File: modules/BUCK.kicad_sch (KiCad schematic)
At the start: 6 parts, among them U4 TPS628502

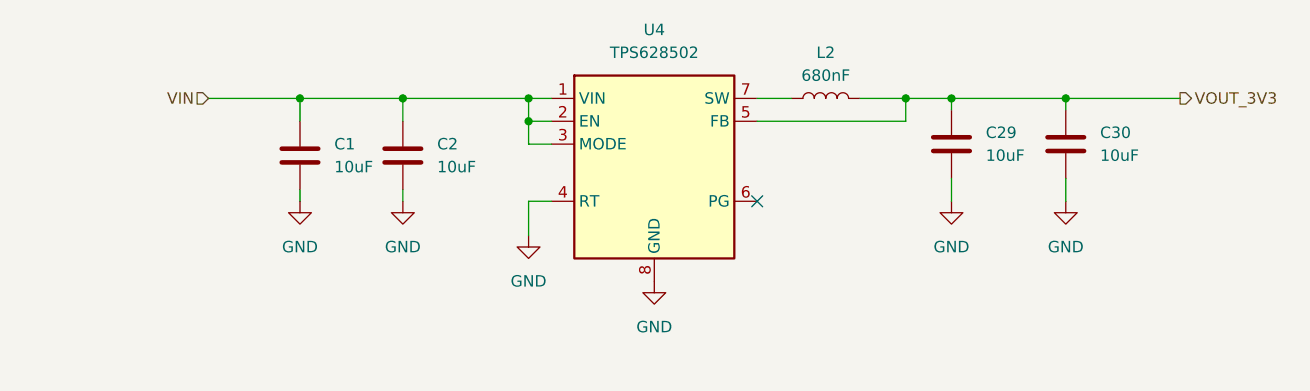
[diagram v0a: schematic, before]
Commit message: Modificaciond de conexiones
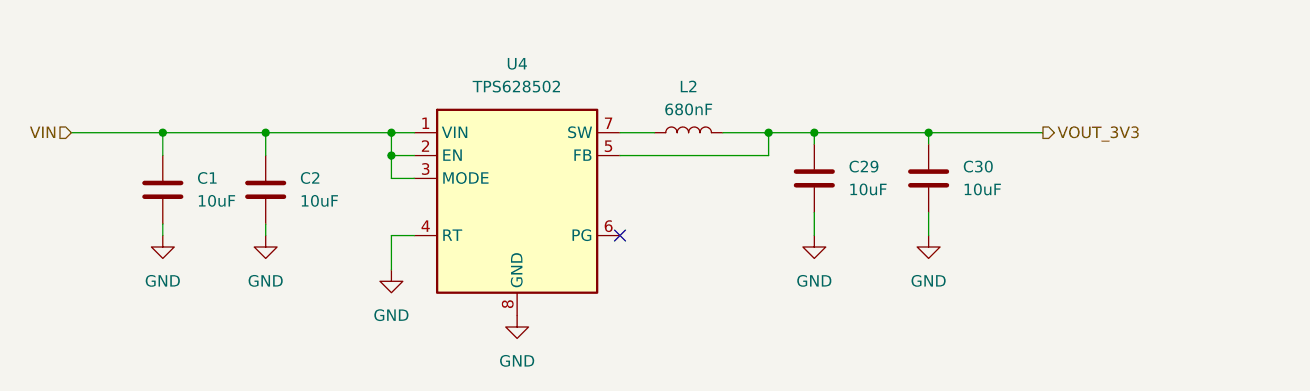
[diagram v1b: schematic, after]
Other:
- moved on the sheet: C1, C2, C29, C30, L2, U4
